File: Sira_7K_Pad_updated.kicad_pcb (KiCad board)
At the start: 2 copper layers, 136.5 x 85.7 mm, 29 parts, among them J1 AVR-ISP-6, SW1 SW_Push, U1 ATmega32U4-A, U2 PRTR5V0U2X, Y1 Crystal_GND24_Small

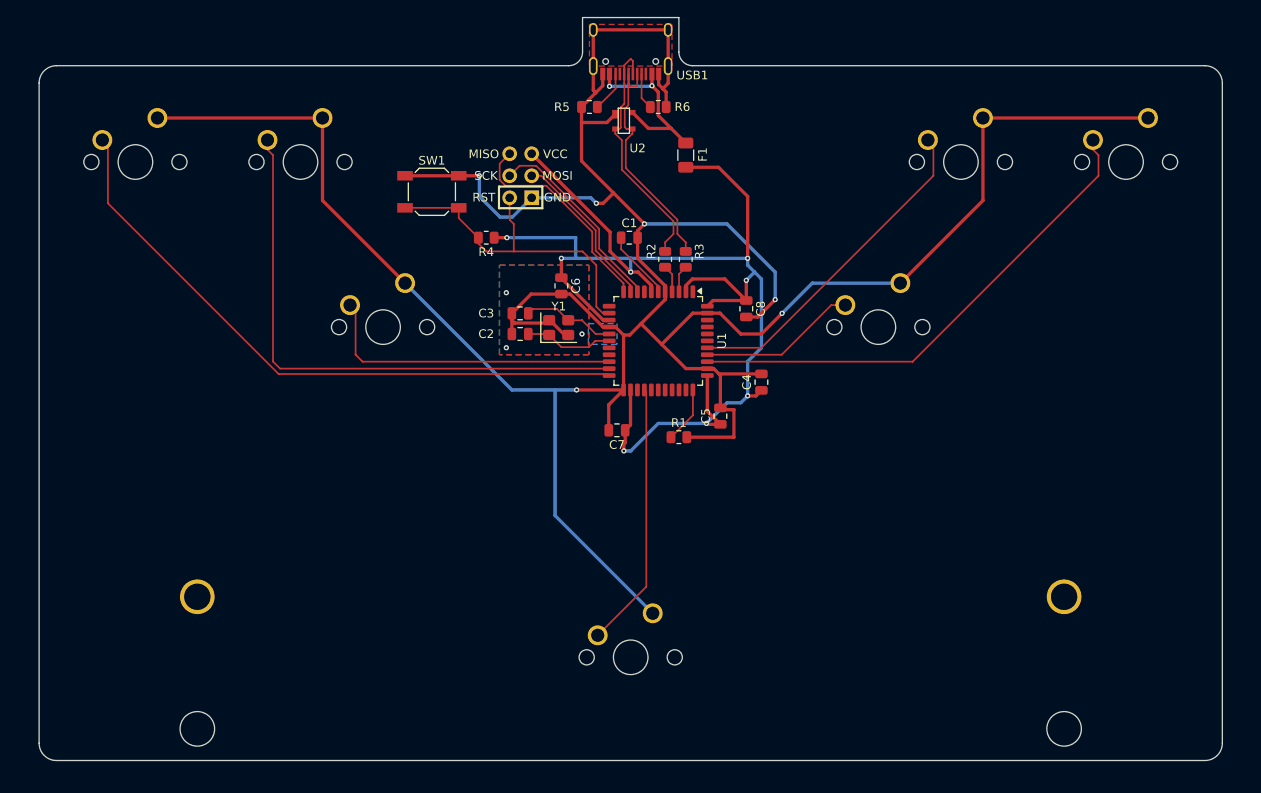
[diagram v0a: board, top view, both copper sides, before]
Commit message: almost finished routing and cleaning up the pcb
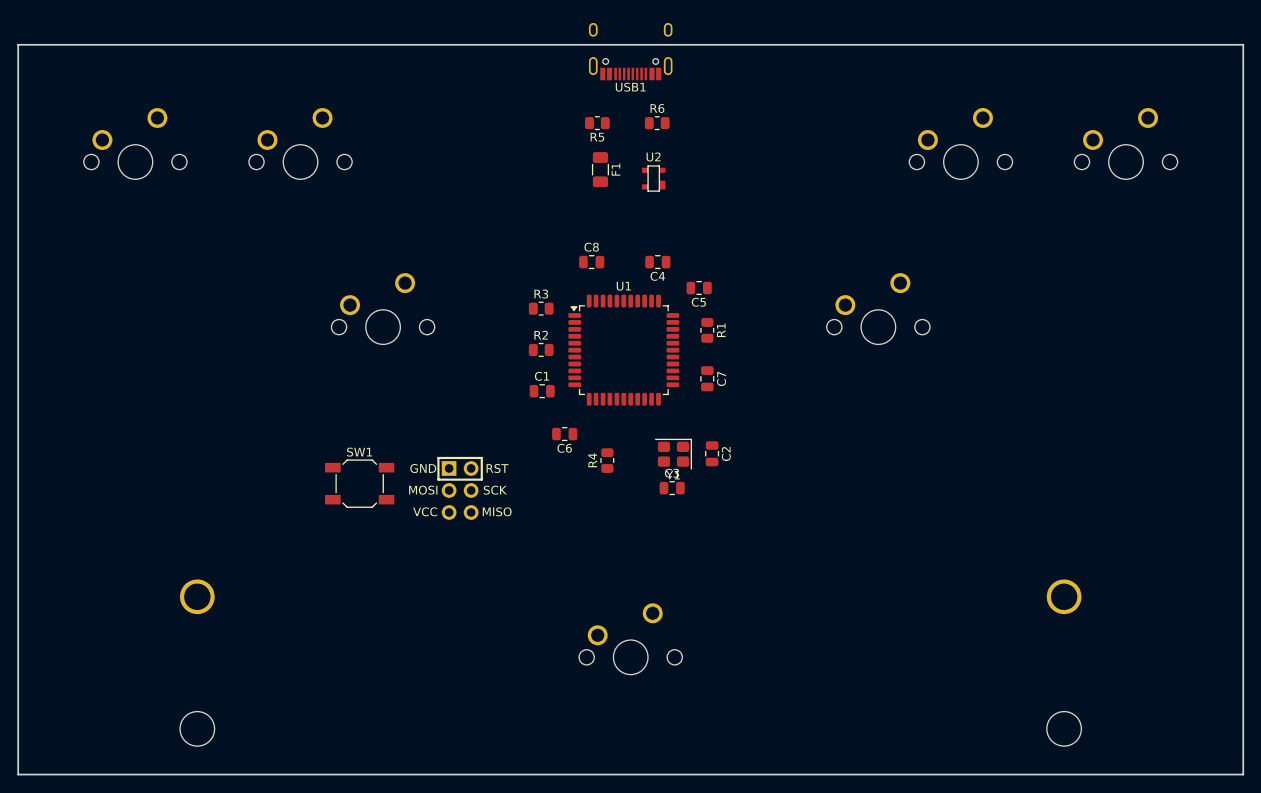
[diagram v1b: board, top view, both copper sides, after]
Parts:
- moved J1 37.0 mm to (128.0, 113.3), turned to 180 degrees
- moved SW1 34.7 mm to (116.4, 112.5)
- moved R4 29.3 mm to (144.9, 109.9), turned to 90 degrees
- moved C3 26.7 mm to (152.4, 113.0), turned to 0 degrees
- moved C2 26.1 mm to (157.0, 109.1), turned to -90 degrees
- moved C1 20.4 mm to (137.4, 101.9)
- moved Y1 19.7 mm to (152.6, 109.1), turned to 180 degrees
- moved R2 19.7 mm to (137.3, 97.1), turned to 0 degrees
- moved C8 18.6 mm to (143.1, 87.0), turned to 0 degrees
- moved C4 18.3 mm to (150.8, 87.0), turned to 180 degrees
- moved C6 17.1 mm to (140.0, 106.8), turned to 180 degrees
- moved R3 15.4 mm to (137.3, 92.3), turned to 0 degrees
- moved C5 15.0 mm to (155.5, 89.9), turned to 180 degrees
- moved R1 12.8 mm to (156.5, 94.8), turned to -90 degrees
- moved C7 12.0 mm to (156.5, 100.4), turned to -90 degrees
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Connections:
- R2 pad 1: DN -> D+
- R2 pad 2: D- -> Net-(U1-D+)
- R3 pad 1: DP -> D-
- R3 pad 2: D+ -> Net-(U1-D-)
- U1 pad 18: unconnected-(U1-PD0-Pad18) -> MX1
- U1 pad 19: unconnected-(U1-PD1-Pad19) -> MX2
- U1 pad 21: MX2 -> MX4
- U1 pad 22: MX1 -> MX6
- U1 pad 25: unconnected-(U1-PD4-Pad25) -> MX5
- U1 pad 3: D- -> Net-(U1-D-)
- U1 pad 36: MX6 -> unconnected-(U1-PF7-Pad36)
- U1 pad 37: MX4 -> unconnected-(U1-PF6-Pad37)
- U1 pad 38: MX5 -> unconnected-(U1-PF5-Pad38)
- U1 pad 4: D+ -> Net-(U1-D+)
- U2 pad 2: DP -> D+
- U2 pad 3: DN -> D-
- USB1 pad 5: DN -> D-
- USB1 pad 6: DP -> D+
- USB1 pad 7: DN -> D-
- USB1 pad 8: DP -> D+
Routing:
- net GND: track 368.2 -> 0.00 mm, vias 9 -> 0
- net +5V: track 151.1 -> 0.00 mm, vias 8 -> 0
- net MX1: track 72.5 -> 0.00 mm
- net MX2: track 64.9 -> 0.00 mm
- net MX6: track 58.4 -> 0.00 mm
- net RESET: track 38.9 -> 0.00 mm
- net MX5: track 37.8 -> 0.00 mm
- net MX3: track 34.7 -> 0.00 mm
- net MX7: track 30.7 -> 0.00 mm
- net DP: track 28.7 -> 0.00 mm
- net DN: track 28.3 -> 0.00 mm
- net MISO: track 25.1 -> 0.00 mm
- net SCK: track 22.4 -> 0.00 mm
- net VCC: track 21.2 -> 0.00 mm, vias 2 -> 0
- net MOSI: track 18.8 -> 0.00 mm
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- removed copper zone on B.Cu, net GND
- removed copper zone on F.Cu, net GND
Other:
- board size 136.5 x 85.7 mm -> 141.3 x 84.2 mm
